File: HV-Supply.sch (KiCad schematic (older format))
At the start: 7 parts, among them U201 DC-DC-Converter

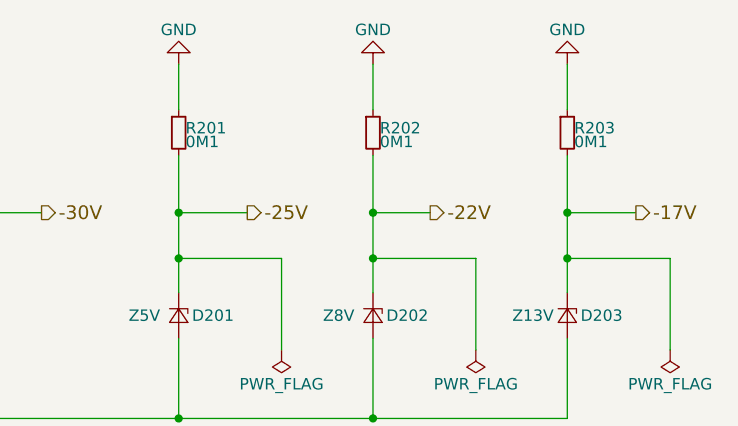
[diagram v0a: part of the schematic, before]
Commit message: switching to more convenient notation of values, e.g. 100K instead of 0M1
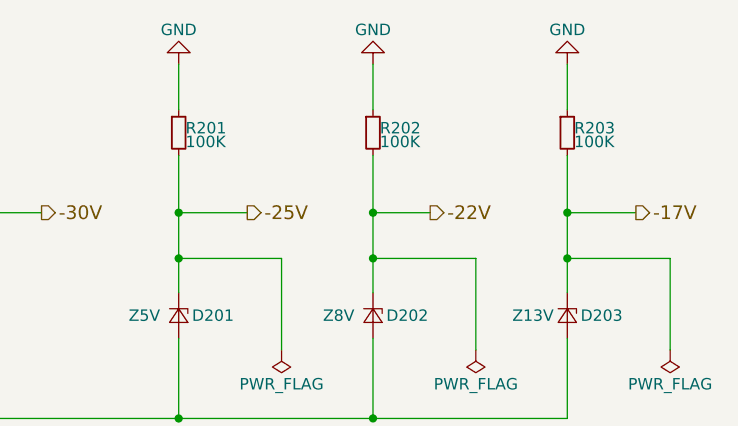
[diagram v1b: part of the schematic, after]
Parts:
- R201, R202, R203: value 0M1 -> 100K
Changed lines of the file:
@@
 P 4450 2050
 F 0 "R201" H 4480 2070 50  0000 L CNN
-F 1 "0M1" H 4480 2010 50  0000 L CNN
+F 1 "100K" H 4480 2010 50  0000 L CNN
 F 2 "Resistors_SMD:R_0805_HandSoldering" H 4450 2050 50  0001 C CNN
 F 3 "" H 4450 2050 50  0001 C CNN
@@
 P 5300 2050
 F 0 "R202" H 5330 2070 50  0000 L CNN
-F 1 "0M1" H 5330 2010 50  0000 L CNN
+F 1 "100K" H 5330 2010 50  0000 L CNN
 F 2 "Resistors_SMD:R_0805_HandSoldering" H 5300 2050 50  0001 C CNN
 F 3 "" H 5300 2050 50  0001 C CNN
@@
 P 6150 2050
 F 0 "R203" H 6180 2070 50  0000 L CNN
-F 1 "0M1" H 6180 2010 50  0000 L CNN
+F 1 "100K" H 6180 2010 50  0000 L CNN
 F 2 "Resistors_SMD:R_0805_HandSoldering" H 6150 2050 50  0001 C CNN
 F 3 "" H 6150 2050 50  0001 C CNN
